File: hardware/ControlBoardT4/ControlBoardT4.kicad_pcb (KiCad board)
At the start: 2 copper layers, 68.6 x 55.2 mm, 23 parts, among them J1 RC, J10 BT Switch, J11 AudioJack4, J12 BT, J2 LinAct, J3 sPOT, J4 Other 1 & 2, J5 [Other Connections 1-6], J6 Other 5 & 6, J7 8P8C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

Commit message: Switched direction of the headphone jack
Pointed the headphone jack in the same direction as the RJ45 connector.
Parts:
- moved J11 23.8 mm to (118.7, 86.2), turned to 0 degrees
- moved JP1 16.9 mm to (122.1, 117.9)
- moved R1 13.3 mm to (117.9, 92.0), turned to 0 degrees
- moved JP2 12.8 mm to (122.4, 110.5)
- moved JP3 12.8 mm to (127.0, 110.5)
- moved U2 12.4 mm to (118.0, 96.5)
- moved J9 5.59 mm to (111.2, 86.4)
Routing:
- net GND: track 172.8 -> 208.3 mm, vias 1 -> 0
- net Net-(J11-PadT): track 7.46 -> 31.2 mm
- net +5V: track 160.6 -> 139.1 mm
- net Net-(J11-PadR1): track 14.6 -> 30.7 mm
- net Net-(J12-Pad2): track 71.2 -> 57.4 mm
- net Net-(J7-Pad4): track 52.3 -> 65.3 mm
- net Net-(J7-Pad3): track 55.4 -> 67.6 mm
- net Net-(J9-Pad5): track 39.4 -> 27.2 mm
- net Net-(J10-Pad1): track 51.3 -> 41.3 mm, vias 0 -> 1
- net Net-(J9-Pad7): track 23.9 -> 33.2 mm, vias 1 -> 0
- net Net-(J9-Pad10): track 27.2 -> 18.0 mm
- net Net-(J11-PadS): track 19.2 -> 27.6 mm
- net Net-(J9-Pad8): track 11.7 -> 17.3 mm
- net Net-(J9-Pad12): track 23.5 -> 28.0 mm, vias 1 -> 0

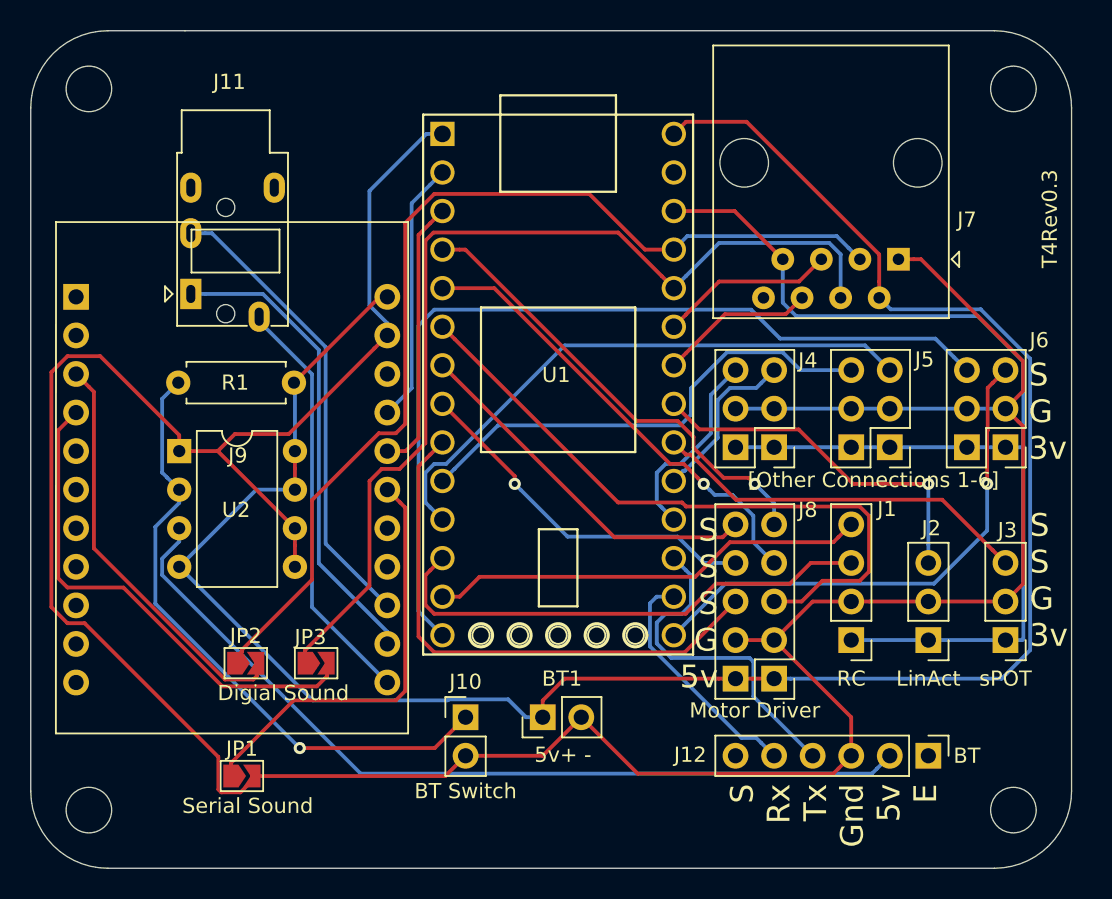
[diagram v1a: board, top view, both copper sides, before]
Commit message: Fixed headphone jack x-axis.
Fixed headphone jack x-axis. Created new PJ320A footprint in 'Useful Modifications' library. Updated schematic to use the new footprint.
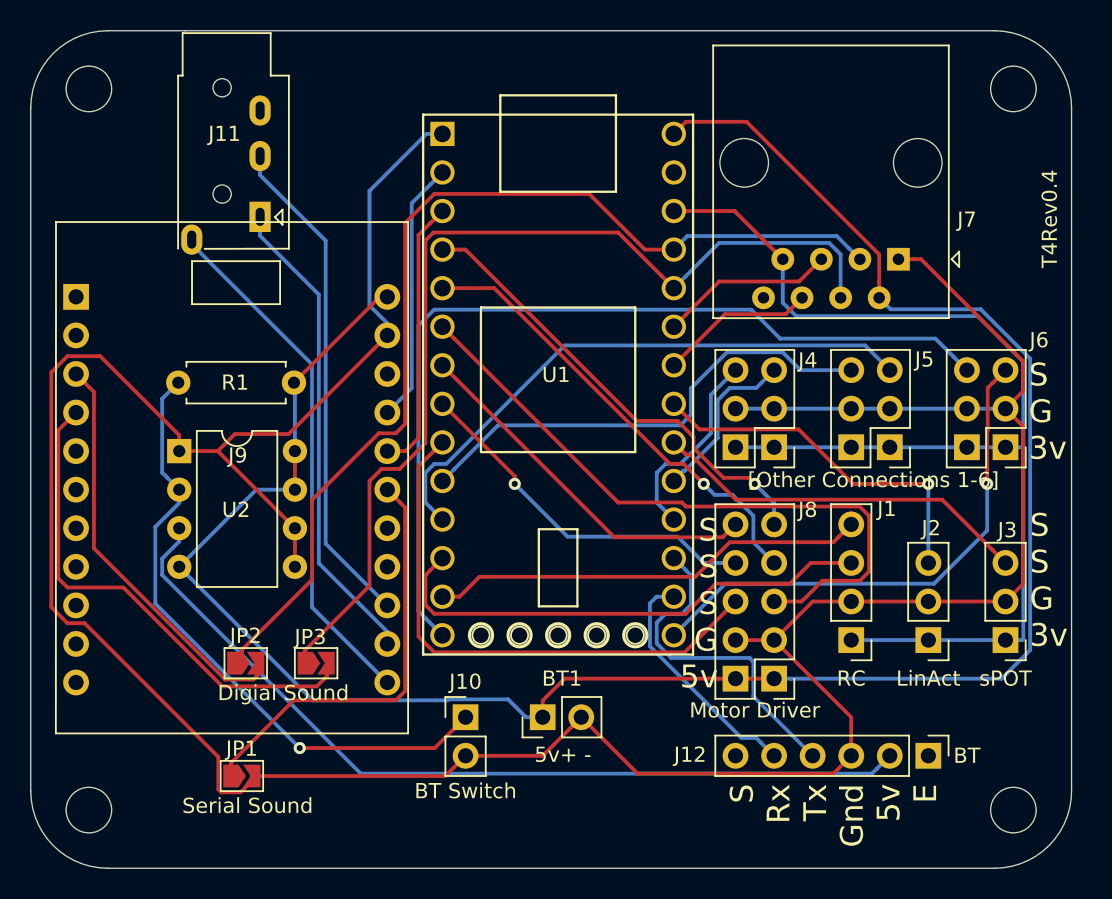
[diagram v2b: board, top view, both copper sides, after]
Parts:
- J11: footprint Connector_Audio:Jack_3.5mm_PJ320E_Horizontal -> Useful Modifications:Jack_3.5mm_PJ320A_Horizontal
- moved J11 5.08 mm to (118.8, 81.1)
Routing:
- net Net-(J11-PadS): track 27.6 -> 34.5 mm
- net Net-(J11-PadR1): track 30.7 -> 33.1 mm
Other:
- board text added: "T4Rev0.4"
- board text removed: "T4Rev0.3"

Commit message: Switched Motor Label moved headphone jack
Switched A and B on motor label. Adjusted the headphone jack holes to allow the headphone jack to plug in further.
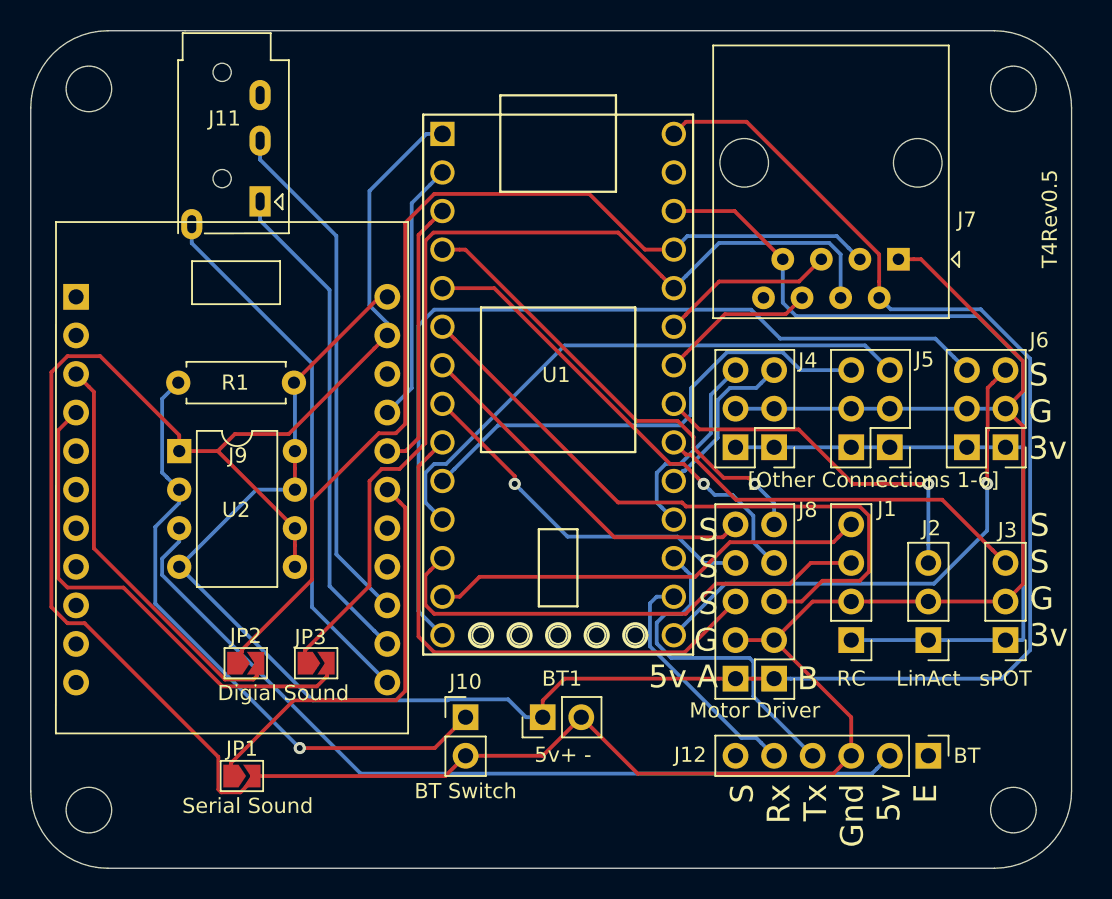
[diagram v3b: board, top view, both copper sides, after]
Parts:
- moved J11 1.02 mm to (118.8, 80.1)
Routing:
- net Net-(J11-PadT): track 31.6 -> 32.6 mm
- net Net-(J11-PadR1): track 33.1 -> 34.1 mm
- net Net-(J11-PadS): track 34.5 -> 35.5 mm
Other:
- board text added: "B"
- board text added: "S S S G 5v A"
- board text added: "T4Rev0.5"
- board text removed: "S S S G 5v"
- board text removed: "T4Rev0.4"
